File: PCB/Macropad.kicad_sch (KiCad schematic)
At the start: 8 parts, among them J1 Conn_01x04_MountingPin, SW1 SW_Push, SW10 RotaryEncoder_Switch, SW2 SW_Push, SW4 SW_Push, SW5 SW_Push, SW6 SW_Push, U1 MOUDLE-SEEEDUINO-XIAO

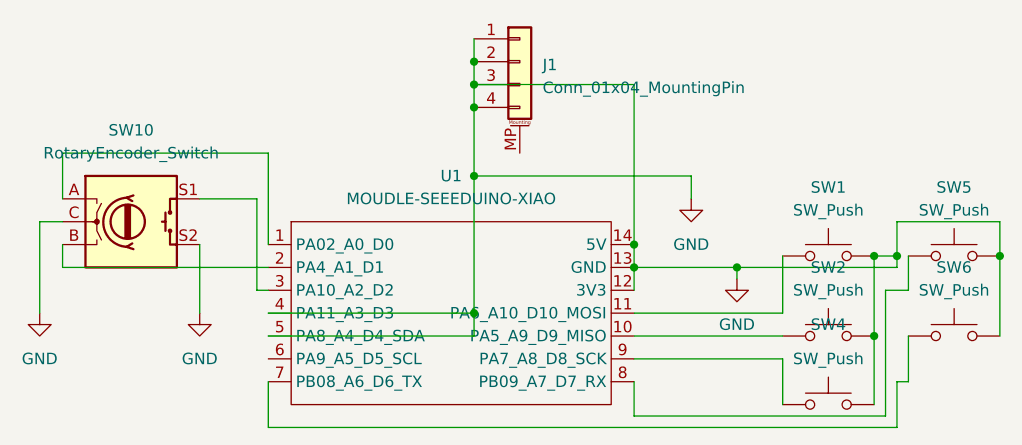
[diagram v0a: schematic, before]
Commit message: Case design update, PCB tweaks
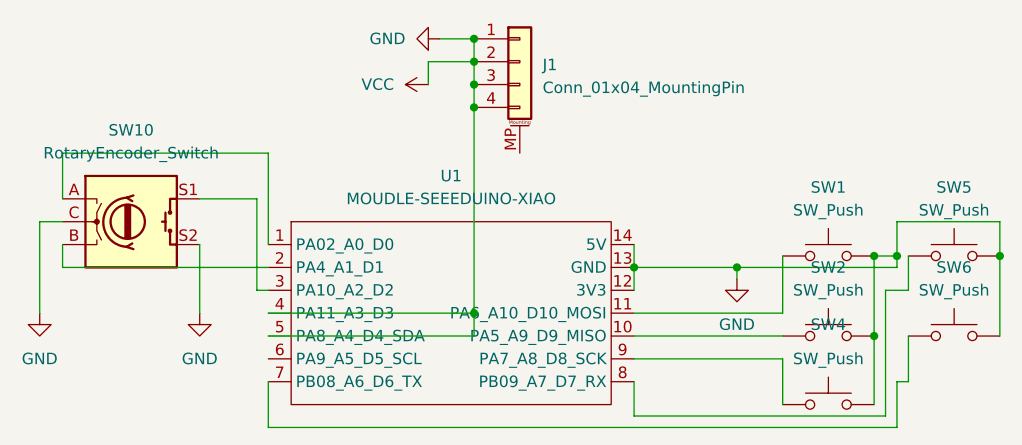
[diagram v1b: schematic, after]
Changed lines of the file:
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@@
 	(paper "A4")
-	(junction
-		(at 128.27 77.47)
-		(diameter 0)
-		(color 0 0 0 0)
-	)
 	(junction
 		(at 110.49 57.15)
@@
 	)
 	(junction
-		(at 110.49 69.85)
+		(at 110.49 54.61)
 		(diameter 0)
 		(color 0 0 0 0)
@@
 	(wire
 		(pts
+			(xy 106.68 54.61) (xy 110.49 54.61)
+		)
+		(stroke
+			(width 0)
+			(type default)
+		)
+	)
+	(wire
+		(pts
 			(xy 110.49 59.69) (xy 110.49 62.23)
 		)
@@
 	(wire
 		(pts
+			(xy 105.41 57.15) (xy 105.41 59.69)
+		)
+		(stroke
+			(width 0)
+			(type default)
+		)
+	)
+	(wire
+		(pts
 			(xy 128.27 87.63) (xy 144.78 87.63)
 		)
@@
 	(wire
 		(pts
-			(xy 110.49 62.23) (xy 110.49 69.85)
+			(xy 110.49 62.23) (xy 110.49 85.09)
 		)
 		(stroke
@@
 	(wire
 		(pts
-			(xy 110.49 69.85) (xy 110.49 85.09)
-		)
-		(stroke
-			(width 0)
-			(type default)
-		)
-	)
-	(wire
-		(pts
 			(xy 110.49 57.15) (xy 110.49 59.69)
 		)
@@
 	(wire
 		(pts
-			(xy 110.49 69.85) (xy 134.62 69.85)
-		)
-		(stroke
-			(width 0)
-			(type default)
-		)
-	)
-	(wire
-		(pts
 			(xy 156.21 96.52) (xy 128.27 96.52)
 		)
@@
 	(wire
 		(pts
+			(xy 110.49 57.15) (xy 105.41 57.15)
+		)
+		(stroke
+			(width 0)
+			(type default)
+		)
+	)
+	(wire
+		(pts
 			(xy 157.48 97.79) (xy 87.63 97.79)
 		)
@@
 	(wire
 		(pts
-			(xy 110.49 59.69) (xy 128.27 59.69)
-		)
-		(stroke
-			(width 0)
-			(type default)
-		)
-	)
-	(wire
-		(pts
-			(xy 134.62 69.85) (xy 134.62 72.39)
-		)
-		(stroke
-			(width 0)
-			(type default)
-		)
-	)
-	(wire
-		(pts
 			(xy 128.27 85.09) (xy 144.78 85.09)
 		)
@@
 		(pts
 			(xy 64.77 67.31) (xy 87.63 67.31)
-		)
-		(stroke
-			(width 0)
-			(type default)
-		)
-	)
-	(wire
-		(pts
-			(xy 128.27 59.69) (xy 128.27 77.47)
 		)
 		(stroke
@@
 	)
 	(symbol
+		(lib_id "power:VCC")
+		(at 105.41 59.69 90)
+		(unit 1)
+		(exclude_from_sim no)
+		(in_bom yes)
+		(on_board yes)
+		(dnp no)
+		(fields_autoplaced yes)
+		(property "Reference" "#PWR05"
+			(at 109.22 59.69 0)
+			(effects
+				(font
+					(size 1.27 1.27)
+				)
+				(hide yes)
+			)
+		)
+		(property "Value" "VCC"
+			(at 101.6 59.6899 90)
+			(effects
+				(font
+					(size 1.27 1.27)
+				)
+				(justify left)
+			)
+		)
+		(property "Footprint" ""
+			(at 105.41 59.69 0)
+			(effects
+				(font
+					(size 1.27 1.27)
+				)
+				(hide yes)
+			)
+		)
+		(property "Datasheet" ""
+			(at 105.41 59.69 0)
+			(effects
+				(font
+					(size 1.27 1.27)
+				)
+				(hide yes)
+			)
+		)
+		(property "Description" "Power symbol creates a global label with name \"VCC\""
+			(at 105.41 59.69 0)
+			(effects
+				(font
+					(size 1.27 1.27)
+				)
+				(hide yes)
+			)
+		)
+		(pin "1"
+		)
+		(instances
+			(project ""
+				(path "/d25eebad-b527-4e16-8248-25ef6acaecf1"
+					(reference "#PWR05")
+					(unit 1)
+				)
+			)
+		)
+	)
+	(symbol
 		(lib_id "XIAO_RP2040:MOUDLE-SEEEDUINO-XIAO")
 		(at 106.68 85.09 0)
@@
 	)
 	(symbol
-		(lib_id "power:GND")
-		(at 134.62 72.39 0)
-		(unit 1)
-		(exclude_from_sim no)
-		(in_bom yes)
-		(on_board yes)
-		(dnp no)
-		(fields_autoplaced yes)
-		(property "Reference" "#PWR04"
-			(at 134.62 78.74 0)
-			(effects
-				(font
-					(size 1.27 1.27)
-				)
-				(hide yes)
-			)
-		)
-		(property "Value" "GND"
-			(at 134.62 77.47 0)
-			(effects
-				(font
-					(size 1.27 1.27)
-				)
-			)
-		)
-		(property "Footprint" ""
-			(at 134.62 72.39 0)
-			(effects
-				(font
-					(size 1.27 1.27)
-				)
-				(hide yes)
-			)
-		)
-		(property "Datasheet" ""
-			(at 134.62 72.39 0)
-			(effects
-				(font
-					(size 1.27 1.27)
-				)
-				(hide yes)
-			)
-		)
-		(property "Description" "Power symbol creates a global label with name \"GND\" , ground"
-			(at 134.62 72.39 0)
-			(effects
-				(font
-					(size 1.27 1.27)
-				)
-				(hide yes)
-			)
-		)
-		(pin "1"
-		)
-		(instances
-			(project ""
-				(path "/d25eebad-b527-4e16-8248-25ef6acaecf1"
-					(reference "#PWR04")
-					(unit 1)
-				)
-			)
-		)
-	)
-	(symbol
 		(lib_id "Switch:SW_Push")
 		(at 149.86 95.25 0)
@@
 					(unit 1)
 				)
+			)
+		)
+	)
+	(symbol
+		(lib_id "power:GND")
+		(at 106.68 54.61 270)
+		(unit 1)
+		(exclude_from_sim no)
+		(in_bom yes)
+		(on_board yes)
+		(dnp no)
+		(fields_autoplaced yes)
+		(property "Reference" "#PWR04"
+			(at 100.33 54.61 0)
+			(effects
+				(font
+					(size 1.27 1.27)
+				)
+				(hide yes)
+			)
+		)
+		(property "Value" "GND"
+			(at 102.87 54.6099 90)
+			(effects
+				(font
+					(size 1.27 1.27)
+				)
+				(justify right)
+			)
+		)
+		(property "Footprint" ""
+			(at 106.68 54.61 0)
+			(effects
+				(font
+					(size 1.27 1.27)
+				)
+				(hide yes)
+			)
+		)
+		(property "Datasheet" ""
+			(at 106.68 54.61 0)
+			(effects
+				(font
+					(size 1.27 1.27)
+				)
+				(hide yes)
+			)
+		)
+		(property "Description" "Power symbol creates a global label with name \"GND\" , ground"
+			(at 106.68 54.61 0)
+			(effects
+				(font
+					(size 1.27 1.27)
+				)
+				(hide yes)
+			)
+		)
+		(pin "1"
+		)
+		(instances
+			(project ""
+				(path "/d25eebad-b527-4e16-8248-25ef6acaecf1"
+					(reference "#PWR04")
+					(unit 1)
+				)

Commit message: Remade PCB and case
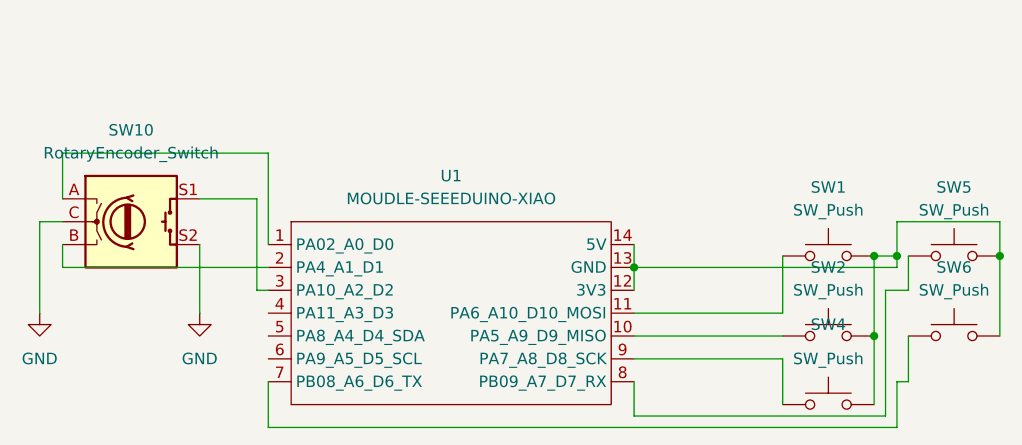
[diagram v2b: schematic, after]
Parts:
- removed J1: Conn_01x04_MountingPin, Connector_PinHeader_2.54mm:PinHeader_1x04_P2.54mm_Vertical, symbol Connector_Generic_MountingPin:Conn_01x04_MountingPin
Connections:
- net GND: no longer SW1.2, SW2.2, SW4.2, SW5.2, SW6.2, U1.12 (3V3), U1.13 (GND), U1.14 (5V), U1.4 (PA11_A3_D3), U1.5 (PA8_A4_D4_SDA)
- new net: SW1.2, SW2.2, SW4.2, SW5.2, SW6.2, U1.12 (3V3), U1.13 (GND), U1.14 (5V)
